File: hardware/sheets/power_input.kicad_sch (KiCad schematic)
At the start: 0 parts

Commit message: feat(hw): draft power_input sheet -- fused, reverse-protected, filtered 12V input
Single 12 V feed -> 10 A fuse -> P-FET reverse-polarity block -> Zener/TVS clamp
-> pi filter -> VBAT, with a Schottky to VLOGIC_IN. Authored as text; every
lib_symbols entry extracted verbatim from the stock KiCad 10 libraries.

P-FET orientation is deliberate and is the opposite of the plan's Task 3 prose:
DRAIN faces the fused side, SOURCE faces the load (VBAT_PROT). A P-channel body
diode conducts drain->source, so this orientation is self-starting (the body
diode pulls VBAT_PROT up, R1 holds the gate near GND, Vgs ~= -11.4 V) and blocks
the reverse path. Wired the other way, reverse polarity passes straight through
the body diode. A text box on the sheet records this and flags the SQJ415EP
datasheet pinout check before fabrication.

Q1 uses Transistor_FET:Q_PMOS_GSD rather than Device:Q_PMOS: the latter numbers
its pins with the letters D/G/S, which map to no stock footprint.

Netlist-verified (hardware/output/netlist.net), exact membership:
  FEED_P      J1.1 F1.1
  FEED_FUSED  F1.2 Q1.3[D]
  VBAT_PROT   Q1.2[S] D1.1[K] D2.1[A1] C1.1 L1.1
  VBAT        L1.2 C2.1 C3.1 C4.1 D3.2[A]
  VLOGIC_IN   D3.1[K] C5.1
  Q1_G        Q1.1[G] R1.1 D1.2[A]
  GND         J1.2 R1.2 D2.2[A2] C1.2 C2.2 C3.2 C4.2 C5.2

ERC parses with 3 violations, all out of this file's scope: one
power_pin_not_driven on GND (no PWR_FLAG in the project yet) and two
hier_label_mismatch for VBAT/VLOGIC_IN (the parent sheet symbol has no matching
sheet pins). No no-connect flags were added to hide anything.

Not drawn, text notes left instead: the common-mode choke (it needs the input
return through the same core, which splits GND) and the DNP second feed plus
second Schottky (spec 4.4, footprints only).

Co-Authored-By: Claude Opus 5 <noreply@anthropic.com>
Claude-Session: https://claude.ai/code/session_01Bkq7QP4he4cdfxkUNzx7DL
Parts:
- added C1, C2, C5: 100nF, symbol Device:C
- added C3: 220uF, symbol Device:C_Polarized
- added C4: 1uF, symbol Device:C
- added D1: 12V, symbol Device:D_Zener
- added D2: SMBJ24A, symbol Device:D_TVS
- added D3: Schottky 40V, symbol Device:D_Schottky
- added F1: 10A, symbol Device:Fuse
- added J1: PWR (SS1.5 2-way), symbol Connector:Conn_01x02_Pin
- added L1: 10uH, symbol Device:L
- added Q1: SQJ415EP, symbol Transistor_FET:Q_PMOS_GSD
- added R1: 1M, symbol Device:R
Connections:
- new net FEED_FUSED: F1.2, Q1.3 (D)
- new net FEED_P: F1.1, J1.1 (Pin_1)
- new net GND: C1.2, C2.2, C3.2, C4.2, C5.2, D2.2 (A2), J1.2 (Pin_2), R1.2
- new net Q1_G: D1.2 (A), Q1.1 (G), R1.1
- new net VBAT: C2.1, C3.1, C4.1, D3.2 (A), L1.2
- new net VBAT_PROT: C1.1, D1.1 (K), D2.1 (A1), L1.1, Q1.2 (S)
- new net VLOGIC_IN: C5.1, D3.1 (K)

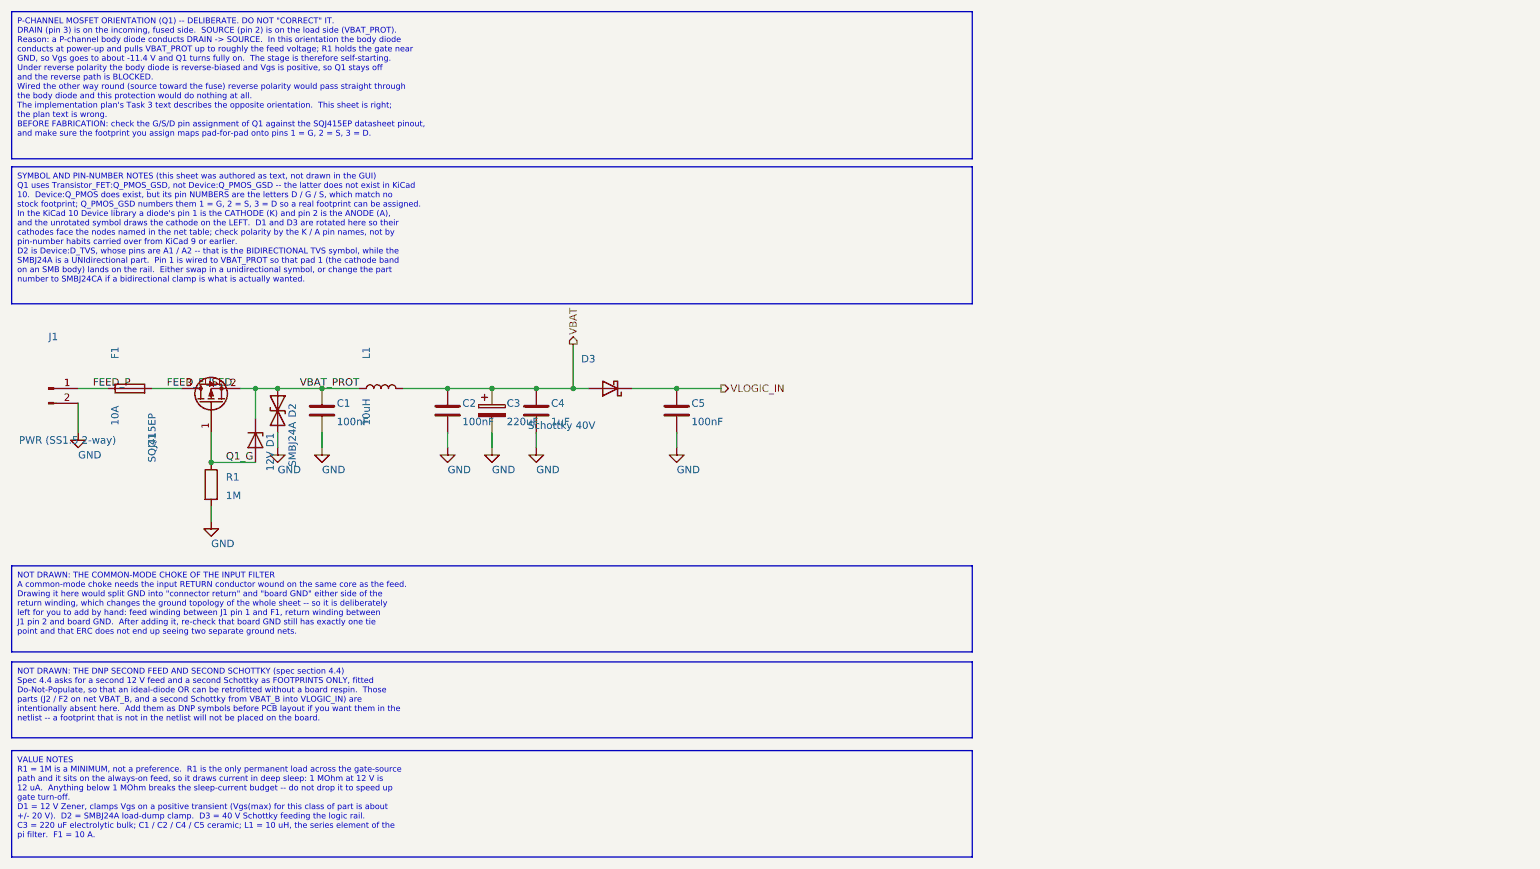
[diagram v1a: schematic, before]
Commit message: feat(hw): add the CM choke to power_input and split the ground net
Order is fuse -> reverse-polarity FET -> TVS -> CM choke -> pi filter -> bulk.
The TVS precedes the choke because surge clamping degrades with series inductance
between the entry point and the clamp; the choke precedes the pi filter because
the common-mode noise being blocked originates inside the board (the boost
converter), so the choke belongs between the switcher and the harness.

New parts:
  L2  Device:L_Coupled, "CM choke" -- pins 1/2 = winding A (feed),
      pins 3/4 = winding B (return)
  R2  0R link across winding A
  R3  0R link across winding B
Fit EITHER L2 OR R2+R3. The links give the simple tied-ground case for the first
prototype and the choke footprint is present either way, so fitting a real choke
later needs no board revision.

THE GROUND IS NOW SPLIT. GND_IN (connector side) and GND (board side) are two
separate nets joined only through choke winding B. J1 pin 2, the TVS anode and
the gate-resistor return all move from GND to GND_IN: they are the protection
group and must reference the ground the surge actually arrives on, and R1 in
particular must reference the return the battery is connected to or the
reverse-polarity behaviour is referenced to the wrong node. GND_IN is a LOCAL
label, never a power symbol -- a second power symbol named GND would merge the
two returns globally and silently defeat the arrangement.

Netlist-verified (hardware/output/netlist.net), 9 nets:
  FEED_P      J1.1 F1.1                          unchanged
  FEED_FUSED  F1.2 Q1.3[D]                       unchanged
  VBAT_PROT   Q1.2[S] D1.1[K] D2.1[A1] L2.1 R2.1 C1/L1 left this net
  VBAT_F      L2.2 R2.2 C1.1 L1.1                new
  VBAT        L1.2 C2.1 C3.1 C4.1 D3.2[A]        unchanged
  VLOGIC_IN   D3.1[K] C5.1                       unchanged
  Q1_G        Q1.1[G] R1.1 D1.2[A]               unchanged
  GND_IN      J1.2 D2.2[A2] R1.2 L2.3 R3.1       new
  GND         L2.4 R3.2 C1.2 C2.2 C3.2 C4.2 C5.2 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
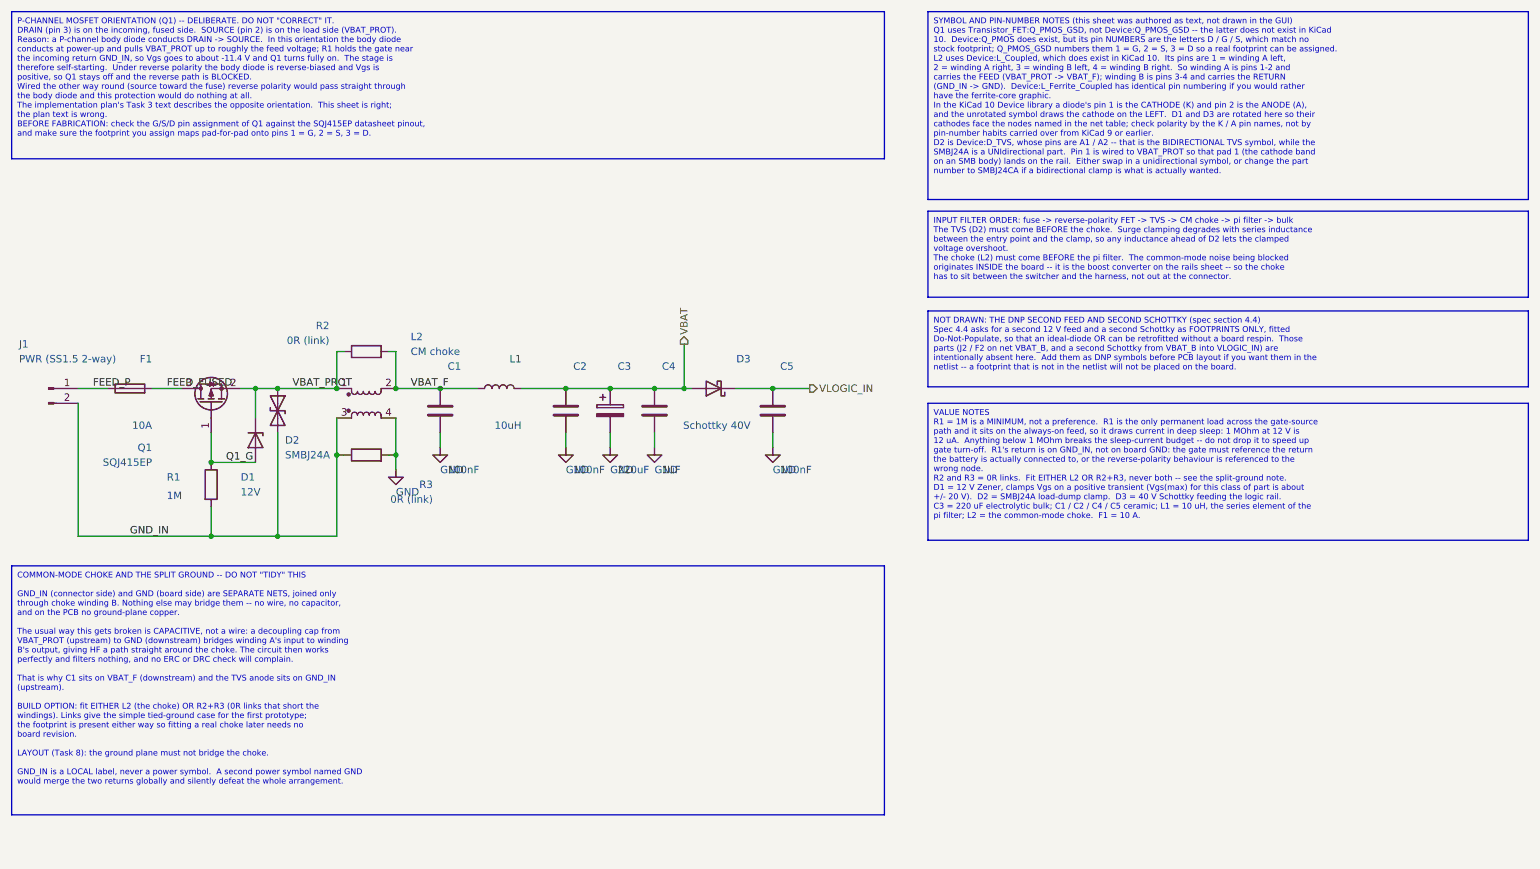
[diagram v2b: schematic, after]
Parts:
- added L2: CM choke, symbol Device:L_Coupled
- added R2, R3: 0R (link), symbol Device:R
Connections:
- net GND: now also L2.4, R3.2; no longer D2.2 (A2), J1.2 (Pin_2), R1.2
- net VBAT_PROT: now also L2.1, R2.1; no longer C1.1, L1.1
- new net GND_IN: D2.2 (A2), J1.2 (Pin_2), L2.3, R1.2, R3.1
- new net VBAT_F: C1.1, L1.1, L2.2, R2.2
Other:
- moved on the sheet: C1, C2, C3, C4, C5, D3, L1
